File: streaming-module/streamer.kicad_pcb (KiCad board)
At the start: 4 copper layers, 75 x 97.3 mm, 47 parts, among them J2 Conn_01x04, J3 HS HS91L02W2C01, J4 Conn_01x15, J6 Conn_02x13_Odd_Even, P1 USB_C_Plug_USB2.0, SW1 RotaryEncoder_Switch, U1 ESP32-S3-WROOM-1, U2 IRM-90-24, U4 SRV05-4, U6 TPS54202DDC, Y1 32k, Y2 22.5792M

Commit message: WIP
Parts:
- removed FL1: Choke_CommonMode_PulseElectronics_PH9455x156NL, Inductor_THT:L_CommonMode_PulseElectronics_PH9455xxx6NL_2
- added C7: C_Polarized, Capacitor_THT:CP_Radial_D8.0mm_P3.50mm, F.Cu at (82.8, 41.6)
- added F1: Fuse, Fuse:Fuse_2512_6332Metric, B.Cu at (26.2, 117.0)
- added J5: Conn_01x01, Connector_Wire:SolderWirePad_1x01_SMD_4x8mm, B.Cu at (79.1, 51.5)
- added J7: Conn_01x16, components:5034801600, B.Cu at (78.6, 59.0)
- added J8: Conn_01x01, Connector_Wire:SolderWire-1.5sqmm_1x01_D1.7mm_OD3mm, F.Cu at (24.1, 97.6)
- added R21: 8.2, Resistor_SMD:R_1206_3216Metric, B.Cu at (75.5, 40.8)
- C1, C25, C26, C27, C28, C33, C6, D1, D2, J2, J3, R1, R15, R18, R19, R20, R5, R6, R7, R8, U6, Y2: moved to B.Cu
- J4: value Conn_01x15 -> Conn_01x01; footprint Connector_PinHeader_1.00mm:PinHeader_1x15_P1.00mm_Vertical -> Connector_Wire:SolderWirePad_1x01_SMD_4x8mm; moved to B.Cu
- J6: value Conn_02x13_Odd_Even -> Conn_01x01; footprint hw-footprints:GT-B0802 FSR 51-26 -> Connector_Wire:SolderWire-1.5sqmm_1x01_D1.7mm_OD3mm
- L5: footprint Inductor_SMD:L_APV_ANR5040 -> Inductor_SMD:L_APV_ANR6028; moved to B.Cu
- moved D1 103.8 mm to (51.3, 67.0), turned to 180 degrees
- moved J6 102.7 mm to (24.1, 108.9), turned to 0 degrees
- moved C6 101.8 mm to (49.5, 98.5), turned to 180 degrees
- moved D2 99.0 mm to (53.7, 56.0)
- moved Y2 98.3 mm to (49.9, 95.8), turned to 90 degrees
- moved R15 90.4 mm to (54.0, 92.6), turned to 90 degrees
- moved R1 86.9 mm to (54.2, 89.7), turned to 180 degrees
- moved C1 85.7 mm to (54.2, 88.6), turned to 0 degrees
- moved J4 75.5 mm to (79.0, 46.6), turned to 90 degrees
- moved C26 56.1 mm to (66.3, 65.5)
- moved C33 54.9 mm to (71.8, 64.5)
- moved C27 54.0 mm to (66.2, 63.6)
- moved L5 53.7 mm to (61.0, 62.7), turned to -90 degrees
- moved C25 53.4 mm to (69.9, 63.0)
- moved R20 52.9 mm to (72.6, 62.5), turned to -90 degrees
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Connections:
- J4 pad 1: +3V3 -> +24V
- J6 pad 1: +24V -> Net-(J6-Pin_1)
- U2 pad 4: Net-(U2--Vout) -> GND
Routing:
- net Net-(U1-IO4): track 50.8 -> 2.28 mm, vias 2 -> 1
- net Net-(U1-IO6): track 47.9 -> 2.10 mm, vias 2 -> 1
- net Net-(U1-IO5): track 44.6 -> 1.75 mm, vias 2 -> 1
- net GND: track 52.8 -> 19.9 mm, vias 32 -> 14
- net Net-(J8-Pin_1): track 0.00 -> 30.5 mm
- net Net-(D1-A): track 20.1 -> 0.00 mm
- net /CC2: track 19.7 -> 0.00 mm, vias 3 -> 0
- net +3V3: track 32.6 -> 13.9 mm, vias 13 -> 7
- net /EN: track 15.3 -> 0.00 mm, vias 2 -> 0
- net /I2S_MCLK: track 12.9 -> 0.00 mm, vias 2 -> 0
- net /EXP_IO2: track 11.0 -> 0.00 mm, vias 1 -> 0
- net /VBUS_D: track 16.0 -> 5.46 mm, vias 9 -> 3
- net /D-: track 10.3 -> 0.00 mm, vias 2 -> 0
- net /CC1: track 10.00 -> 0.00 mm, vias 2 -> 0
- net /D+: track 9.39 -> 0.02 mm, vias 2 -> 0
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- added copper zone on B.Cu, net +3V3
- added copper zone on B.Cu, net GND
- added copper zone on F.Cu, net GND
- added copper zone on In1.Cu, net GND
- added copper zone on In2.Cu, net GND
- added copper zone on B.Cu, net Net-(U6-SW)
- removed copper zone on B.Cu, net +24V
- removed copper zone on F.Cu, net +3V3
- removed copper zone on F.Cu, net /VBUS_D
- removed copper zone on F.Cu, net Net-(U6-SW)
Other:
- board size 75 x 97.3 mm -> 65 x 100.6 mm
- board text removed: "3V3"
- board text removed: "A"
- board text removed: "B"
- board text removed: "GND"
- board text removed: "SCL"
- board text removed: "SDA"

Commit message: wip
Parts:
- removed C6: 100n, Capacitor_SMD:C_0402_1005Metric
- removed R15: 22, Resistor_SMD:R_0402_1005Metric
- removed R8: 4k7, Resistor_SMD:R_0402_1005Metric
- removed Y2: 22.5792M, Crystal:Crystal_SMD_3225-4Pin_3.2x2.5mm
- added N1: amp board, components:virtual_component, F.Cu at (22.1, 25.2)
- J2, J3, P1: moved to F.Cu
- J4: value Conn_01x01 -> AMP_24V
- J5: value Conn_01x01 -> AMP_GND
- moved J3 114.7 mm to (51.7, 127.6), turned to 90 degrees
- moved J2 97.2 mm to (65.2, 127.6), turned to 90 degrees
- moved R18 94.3 mm to (75.0, 35.9), turned to -90 degrees
- moved R7 85.8 mm to (82.4, 36.2), turned to 0 degrees
- moved R6 82.4 mm to (75.1, 77.5), turned to -90 degrees
- moved R5 81.4 mm to (76.1, 77.5), turned to -90 degrees
- moved C1 27.5 mm to (75.4, 106.2), turned to -90 degrees
- moved R1 26.1 mm to (74.4, 106.2), turned to 90 degrees
- moved R16 24.4 mm to (76.2, 37.0), turned to -90 degrees
- moved R17 23.1 mm to (77.2, 37.0), turned to -90 degrees
- moved D1 19.6 mm to (68.1, 56.8), turned to 90 degrees
- moved D2 18.7 mm to (72.1, 59.3), turned to 0 degrees
- moved C3 18.3 mm to (78.0, 100.8), turned to 0 degrees
- moved C4 15.1 mm to (71.0, 102.5)
- moved C5 15.1 mm to (65.8, 102.5)
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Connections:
- C7 pad 1: +24V -> Net-(J4-Pin_1)
- C7 pad 2: GND -> GNDPWR
- J4 pad 1: +24V -> Net-(J4-Pin_1)
- J5 pad 1: GND -> GNDPWR
- R21 pad 2: +24V -> Net-(J4-Pin_1)
- U1 pad 15: /CLK_EN -> unconnected-(U1-IO3-Pad15)
- U1 pad 31: unconnected-(U1-IO38-Pad31) -> /AMP_~{PDN}
- U1 pad 7: /I2S_MCLK -> unconnected-(U1-IO7-Pad7)
- U2 pad 4: GND -> GNDPWR
- U4 pad 4: /CC2 -> /CC1
- U4 pad 6: /CC1 -> /CC2
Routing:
- net GND: track 19.9 -> 117.0 mm, vias 14 -> 55
- net /D-: track 0.00 -> 90.6 mm
- net /D+: track 0.02 -> 88.6 mm
- net /SDA: track 0.00 -> 84.0 mm, vias 0 -> 4
- net /SCL: track 0.00 -> 83.0 mm, vias 0 -> 2
- net /AMP_IO1: track 0.00 -> 55.8 mm, vias 0 -> 2
- net /EXP_IO1: track 0.00 -> 53.5 mm, vias 0 -> 1
- net /EXP_IO2: track 0.00 -> 52.0 mm, vias 0 -> 1
- net /AMP_IO2: track 0.00 -> 44.0 mm, vias 0 -> 2
- net /SDIN: track 0.00 -> 34.8 mm, vias 0 -> 2
- net GNDPWR: track 0.00 -> 29.4 mm, vias 0 -> 16
- net /AMP_~{PDN}: track 0.00 -> 28.8 mm, vias 0 -> 2
- net /LRCLK: track 0.00 -> 26.9 mm
- net /SCLK: track 0.00 -> 24.4 mm
- net Net-(U1-IO6): track 2.10 -> 24.1 mm, vias 1 -> 2
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- added copper zone on In1.Cu, net +3V3
- added copper zone on B.Cu, net GNDPWR
- added copper zone on F.Cu, net GNDPWR
- added copper zone on B.Cu, net Net-(D1-A)
- added copper zone on In1.Cu, net Net-(D1-A)
- added copper zone on B.Cu, net Net-(U2-+Vout)
- removed copper zone on In1.Cu, net GND
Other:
- board size 65 x 100.6 mm -> 65 x 104.1 mm

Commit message: WIP
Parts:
- removed R21: 8.2, Resistor_SMD:R_1206_3216Metric
- added C10: 22u 6.3V, Capacitor_SMD:C_0805_2012Metric, B.Cu at (54.1, 61.9)
- added C11: 100n, Capacitor_SMD:C_0402_1005Metric, B.Cu at (54.8, 63.7)
- added C12: 100n, Capacitor_SMD:C_0402_1005Metric, B.Cu at (53.5, 68.5)
- added C13: 100n, Capacitor_SMD:C_0402_1005Metric, B.Cu at (64.5, 64.3)
- added C14: 100n, Capacitor_SMD:C_0402_1005Metric, B.Cu at (72.4, 61.8)
- added C15: 100n, Capacitor_SMD:C_0402_1005Metric, B.Cu at (72.4, 70.2)
- added C16: 100n, Capacitor_SMD:C_0402_1005Metric, B.Cu at (72.4, 65.9)
- added C6: 4n7, Capacitor_SMD:C_0603_1608Metric, B.Cu at (52.9, 64.8)
- added C8: 68n, Capacitor_SMD:C_1206_3216Metric, B.Cu at (50.9, 65.6)
- added FB5: 50R@100MHz, Inductor_SMD:L_1206_3216Metric, B.Cu at (77.3, 43.2)
- added R2: 680, Resistor_SMD:R_0402_1005Metric, B.Cu at (53.1, 66.7)
- added R22: 22k, Resistor_SMD:R_0402_1005Metric, B.Cu at (51.5, 68.5)
- added R23: 22, Resistor_SMD:R_0402_1005Metric, B.Cu at (71.0, 79.1)
- added R24: 22, Resistor_SMD:R_0402_1005Metric, B.Cu at (72.2, 79.1)
- added R25: 22, Resistor_SMD:R_0402_1005Metric, B.Cu at (59.2, 81.8)
- added R26: 22, Resistor_SMD:R_0402_1005Metric, B.Cu at (65.3, 66.4)
- added R27: 22, Resistor_SMD:R_0402_1005Metric, B.Cu at (65.3, 67.4)
- added R28: 22, Resistor_SMD:R_0402_1005Metric, B.Cu at (65.3, 68.3)
- added R29: 22, Resistor_SMD:R_0402_1005Metric, B.Cu at (72.4, 69.2)
- added R3: 0, Resistor_SMD:R_0402_1005Metric, B.Cu at (69.8, 68.2)
- added R30: 22, Resistor_SMD:R_0402_1005Metric, B.Cu at (72.4, 60.8)
- added R31: 22, Resistor_SMD:R_0402_1005Metric, B.Cu at (72.4, 65.0)
- added R4: 0, Resistor_SMD:R_0402_1005Metric, B.Cu at (69.8, 60.0)
- added R8: 0, Resistor_SMD:R_0402_1005Metric, B.Cu at (69.8, 63.9)
- added TP1: BFRAME, TestPoint:TestPoint_Pad_2.0x2.0mm, B.Cu at (52.8, 73.0)
- added TP2: UOUT, TestPoint:TestPoint_Pad_2.0x2.0mm, B.Cu at (56.9, 73.0)
- added TP3: COUT, TestPoint:TestPoint_Pad_2.0x2.0mm, B.Cu at (60.9, 73.0)
- added U3: DIR9001PWR, easyeda2kicad:TSSOP-28_L9.7-W4.4-P0.65-LS6.4-BL, B.Cu at (59.7, 65.8)
- added U5: TP74LVC1G157C6, Package_TO_SOT_SMD:SOT-363_SC-70-6, B.Cu at (69.8, 65.5)
- added U7: TP74LVC1G157C6, Package_TO_SOT_SMD:SOT-363_SC-70-6, B.Cu at (69.8, 69.8)
- added U8: TP74LVC1G157C6, Package_TO_SOT_SMD:SOT-363_SC-70-6, B.Cu at (69.8, 61.6)
- added U9: PM2.54-1*3, easyeda2kicad:HDR-TH_3P-P2.54-V-F, F.Cu at (81.0, 34.0)
- J4, J5: footprint Connector_Wire:SolderWirePad_1x01_SMD_4x8mm -> Connector_Wire:SolderWire-2.5sqmm_1x01_D2.4mm_OD3.6mm; moved to F.Cu
- P1: footprint Connector_USB:USB_C_Receptacle_HCTL_HC-TYPE-C-16P-01A -> components:MC-710S-Z13
- moved R7 27.5 mm to (55.3, 40.8), turned to 180 degrees
- moved R18 20.6 mm to (55.3, 42.0), turned to 180 degrees
- moved U4 19.7 mm to (60.8, 41.4), turned to 180 degrees
- moved J5 12.9 mm to (81.6, 40.5), turned to 180 degrees
- moved C25 11.4 mm to (68.8, 54.3)
- moved C28 11.4 mm to (64.4, 52.1)
- moved C33 11.4 mm to (69.2, 57.0)
- moved L5 11.4 mm to (59.9, 53.9)
- moved R19 11.4 mm to (69.7, 55.8)
- moved R20 11.4 mm to (70.0, 50.9)
- moved U6 11.4 mm to (67.5, 52.1)
- moved C26 11.4 mm to (65.2, 56.8)
- moved C27 11.4 mm to (65.2, 54.8)
- moved D1 10.9 mm to (75.9, 49.1)
- moved D2 9.02 mm to (73.2, 50.4), turned to -90 degrees
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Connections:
- P1 pad A6: Net-(U4-IO2) -> Net-(P1-D+-PadA6)
- P1 pad A7: Net-(U4-IO1) -> Net-(P1-D--PadA7)
- P1 pad B6: Net-(U4-IO2) -> Net-(P1-D+-PadA6)
- P1 pad B7: Net-(U4-IO1) -> Net-(P1-D--PadA7)
- R16 pad 1: Net-(U4-IO1) -> Net-(P1-D--PadA7)
- R17 pad 1: Net-(U4-IO2) -> Net-(P1-D+-PadA6)
- U1 pad 20: unconnected-(U1-IO12-Pad20) -> /I2S_MUX
- U1 pad 21: unconnected-(U1-IO13-Pad21) -> /OPT_~{CLK_OK}
- U1 pad 22: unconnected-(U1-IO14-Pad22) -> /OPT_~{AUDIO}
- U1 pad 26: /SDIN -> Net-(U1-IO45)
- U1 pad 34: /LRCLK -> Net-(U1-IO41)
- U1 pad 35: /SCLK -> Net-(U1-IO42)
- U4 pad 1: Net-(U4-IO1) -> /D-
- U4 pad 3: Net-(U4-IO2) -> /D+
- U4 pad 4: /CC1 -> /CC2
- U4 pad 6: /CC2 -> /CC1
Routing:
- net /TOSLINK_IN: track 0.00 -> 54.9 mm, vias 0 -> 1
- net /I2S_MUX: track 0.00 -> 47.7 mm, vias 0 -> 4
- net +3V3: track 23.1 -> 70.0 mm, vias 15 -> 25
- net GND: track 117.0 -> 154.6 mm, vias 55 -> 85
- net /OPT_~{AUDIO}: track 0.00 -> 34.2 mm, vias 0 -> 2
- net /OPT_~{CLK_OK}: track 0.00 -> 33.5 mm, vias 0 -> 2
- net GNDPWR: track 29.4 -> 2.32 mm, vias 16 -> 0
- net /CC1: track 7.65 -> 33.0 mm
- net /CC2: track 10.9 -> 35.8 mm
- net /ESP_LRCLK: track 0.00 -> 21.6 mm, vias 0 -> 2
- net /ESP_SDOUT: track 0.00 -> 21.5 mm, vias 0 -> 2
- net /SDIN: track 34.8 -> 14.1 mm, vias 2 -> 0
- net Net-(P1-D+-PadA6): track 0.00 -> 19.3 mm, vias 0 -> 1
- net /ESP_SCLK: track 0.00 -> 19.1 mm, vias 0 -> 2
- net /LRCLK: track 26.9 -> 9.04 mm
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- added copper zone on B.Cu, net Net-(J4-Pin_1)
- removed copper zone on B.Cu, net GNDPWR
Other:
- board size 65 x 104.1 mm -> 65 x 104.6 mm
- board text added: "+24V"
- board text added: "2mm spcr"
- board text added: "GND"

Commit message: WIP
TODO: Silk PM module. toslink module
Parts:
- P1: footprint components:MC-710S-Z13 -> easyeda2kicad:USB-C-SMD_GT-USB-7058; moved to B.Cu
- moved P1 41.0 mm to (35.6, 28.3), turned to 0 degrees
- moved R17 36.1 mm to (38.1, 38.4), turned to 90 degrees
- moved R16 34.6 mm to (39.2, 38.4), turned to 90 degrees
- moved U9 31.2 mm to (49.8, 33.4)
- moved U4 26.0 mm to (35.4, 36.2), turned to -90 degrees
- moved R7 21.0 mm to (34.3, 39.4), turned to -90 degrees
- moved R18 19.1 mm to (36.4, 39.4), turned to -90 degrees
- moved D1 13.3 mm to (62.6, 48.1), turned to 180 degrees
- moved J5 2.46 mm to (83.8, 41.6)
- moved J4 0.64 mm to (81.1, 45.9)
- moved C7 0.38 mm to (82.8, 50.6)
- moved SW1 0.20 mm to (82.6, 125.4)
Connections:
- P1 pad A6: Net-(P1-D+-PadA6) -> Net-(U4-IO2)
- P1 pad A7: Net-(P1-D--PadA7) -> Net-(U4-IO1)
- P1 pad B6: Net-(P1-D+-PadA6) -> Net-(U4-IO2)
- P1 pad B7: Net-(P1-D--PadA7) -> Net-(U4-IO1)
- R16 pad 1: Net-(P1-D--PadA7) -> /D+
- R16 pad 2: /D- -> Net-(U4-IO2)
- R17 pad 1: Net-(P1-D+-PadA6) -> /D-
- R17 pad 2: /D+ -> Net-(U4-IO1)
- U4 pad 1: /D- -> Net-(U4-IO1)
- U4 pad 3: /D+ -> Net-(U4-IO2)
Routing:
- net Net-(D1-A): track 8.14 -> 63.1 mm, vias 4 -> 8
- net GND: track 154.6 -> 113.6 mm, vias 85 -> 103
- net +3V3: track 70.0 -> 40.4 mm, vias 25 -> 23
- net /CC2: track 35.8 -> 9.91 mm
- net /CC1: track 33.0 -> 10.3 mm
- net Net-(P1-D+-PadA6): track 19.3 -> 0.00 mm, vias 1 -> 0
- net Net-(P1-D--PadA7): track 17.7 -> 0.00 mm, vias 1 -> 0
- net /D-: track 95.4 -> 80.8 mm
- net /TOSLINK_IN: track 54.9 -> 40.4 mm, vias 1 -> 2
- net Net-(U4-IO1): track 0.00 -> 13.9 mm, vias 0 -> 2
- net /D+: track 92.7 -> 79.4 mm
- net Net-(U4-IO2): track 0.00 -> 13.2 mm, vias 0 -> 2
- removed copper zone on In1.Cu, net Net-(D1-A)
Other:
- board size 65 x 104.6 mm -> 66 x 104.6 mm
- board text removed: "2mm spcr"

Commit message: RFM
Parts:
- moved U9 1.11 mm to (50.6, 32.7)
- moved N1 0.50 mm to (22.1, 24.7)
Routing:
- net /TOSLINK_IN: track 40.4 -> 41.6 mm

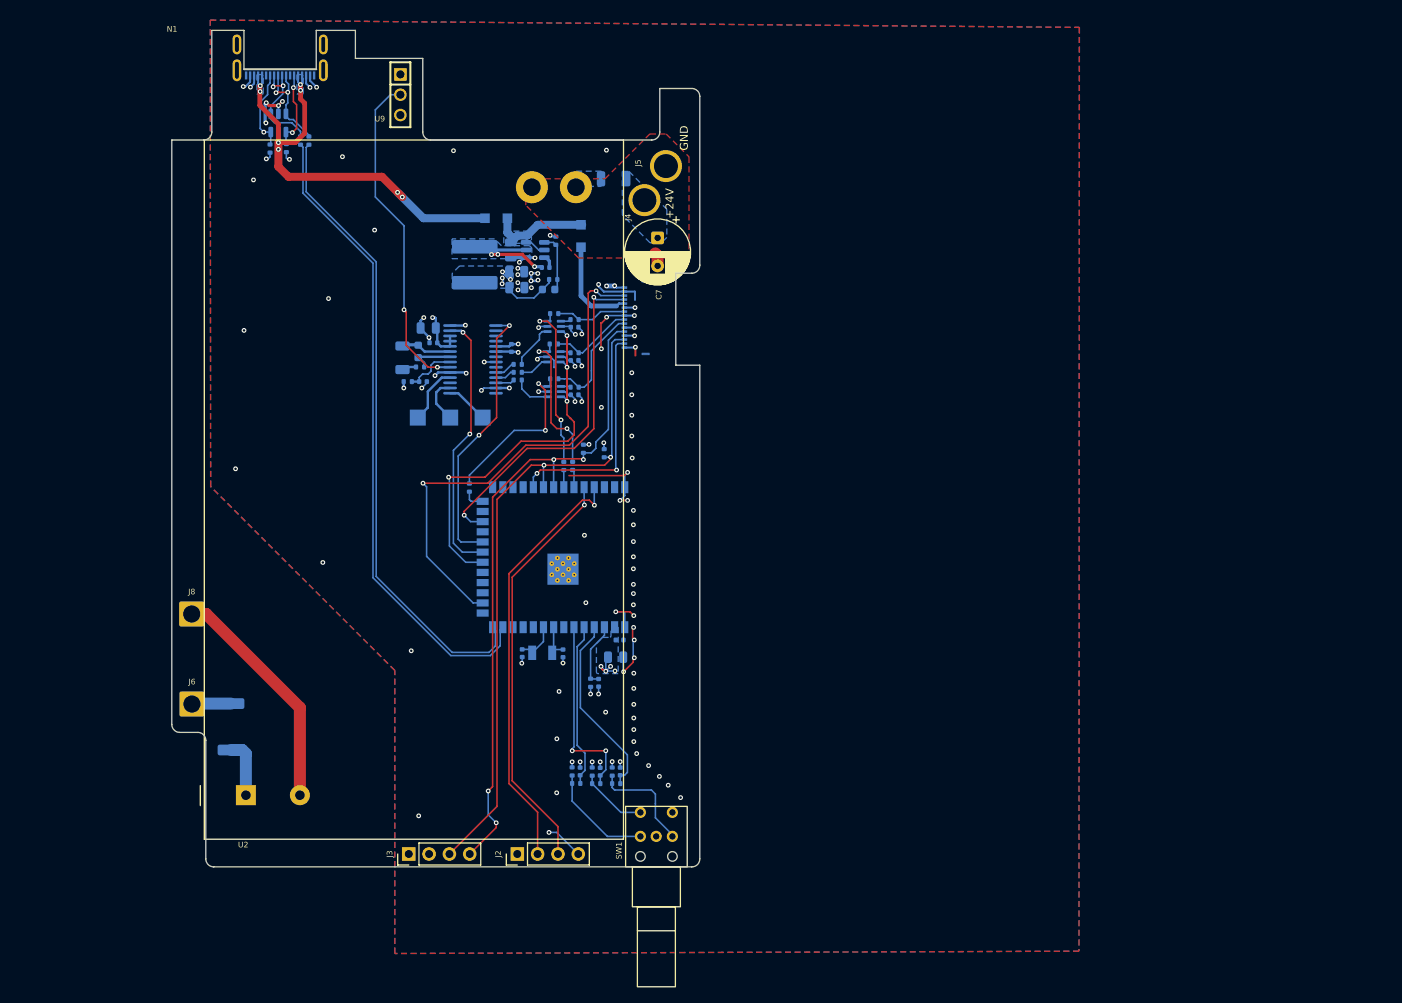
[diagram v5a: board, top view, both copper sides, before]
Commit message: JLC MPN fixes, minor tweaks
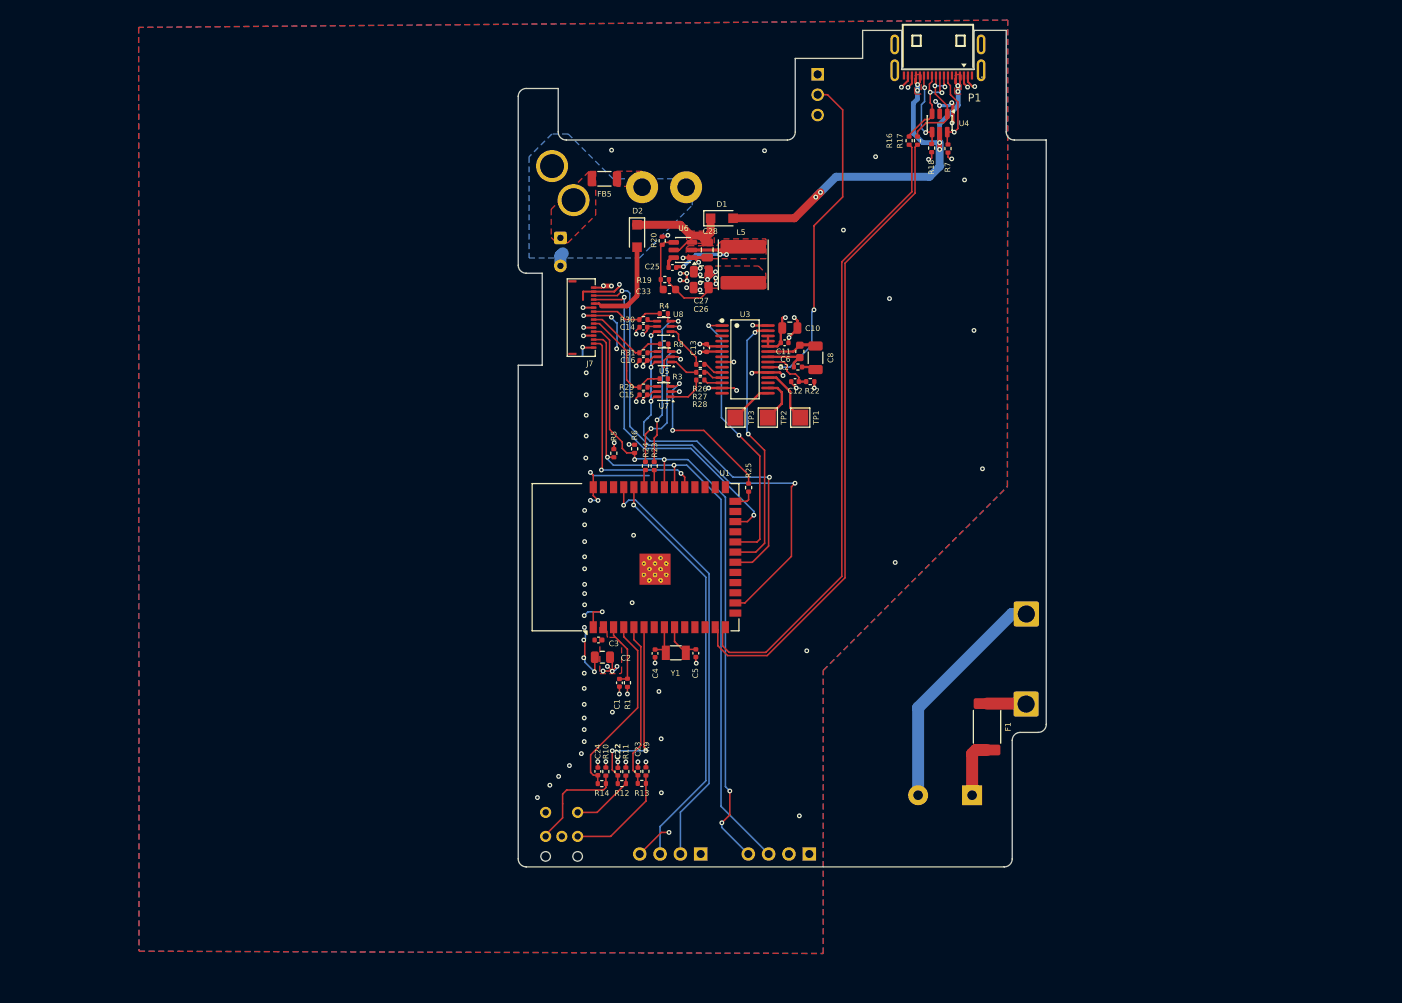
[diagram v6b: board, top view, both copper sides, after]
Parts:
- C1, C10, C11, C12, C13, C14, C15, C16, C2, C22, C23, C24, C25, C26, C27, C28, C3, C33, C4, C5, C6, C8, D1, D2, F1, FB5, J7, L5, P1, R1, R10, R11, R12, R13, R14, R16, R17, R18, R19, R2, R20, R22, R23, R24, R25, R26, R27, R28, R29, R3, R30, R31, R4, R5, R6, R7, R8, R9, TP1, TP2, TP3, U1, U3, U4, U5, U6, U7, U8, Y1: moved to F.Cu
- C7, J2, J3, J4, J5, J6, J8, N1, SW1, U2, U9: moved to B.Cu
- moved N1 109.2 mm to (131.3, 24.7), turned to 180 degrees
- moved J8 104.3 mm to (128.9, 97.6), turned to 180 degrees
- moved J6 104.3 mm to (128.8, 108.9), turned to 180 degrees
- moved F1 94.5 mm to (124.0, 111.7)
- moved U2 90.8 mm to (122.1, 120.2)
- moved R7 84.7 mm to (119.1, 39.4)
- moved U4 82.7 mm to (118.0, 36.2)
- moved P1 82.2 mm to (117.8, 28.3), turned to 180 degrees
- moved R18 80.7 mm to (117.0, 39.4)
- moved R17 77.1 mm to (115.3, 38.4)
- moved R16 75.0 mm to (114.2, 38.4)
- moved U9 52.2 mm to (102.8, 32.7)
- moved C8 51.6 mm to (102.5, 65.6)
- moved R22 50.3 mm to (101.9, 68.5), turned to 180 degrees
- moved J3 50.1 mm to (101.7, 127.6)
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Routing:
- added copper zone on F.Cu, net +3V3
- added copper zone on In2.Cu, net +3V3
- added copper zone on F.Cu, net /VBUS_D
- added copper zone on In1.Cu, net GND
- added copper zone on B.Cu, net GNDPWR
- added copper zone on F.Cu, net Net-(D1-A)
- added copper zone on F.Cu, net Net-(J4-Pin_1)
- added copper zone on F.Cu, net Net-(U2-+Vout)
- added copper zone on F.Cu, net Net-(U6-SW)
- removed copper zone on B.Cu, net +3V3
- removed copper zone on In1.Cu, net +3V3
- removed copper zone on B.Cu, net /VBUS_D
- removed copper zone on In2.Cu, net GND
- removed copper zone on F.Cu, net GNDPWR
- removed copper zone on B.Cu, net Net-(D1-A)
- removed copper zone on B.Cu, net Net-(J4-Pin_1)
- removed copper zone on B.Cu, net Net-(U2-+Vout)
- removed copper zone on B.Cu, net Net-(U6-SW)
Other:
- outline, holes or cut-outs redrawn
